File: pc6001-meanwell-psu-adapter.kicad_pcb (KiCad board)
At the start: 2 copper layers, 223.7 x 84 mm, 4 parts

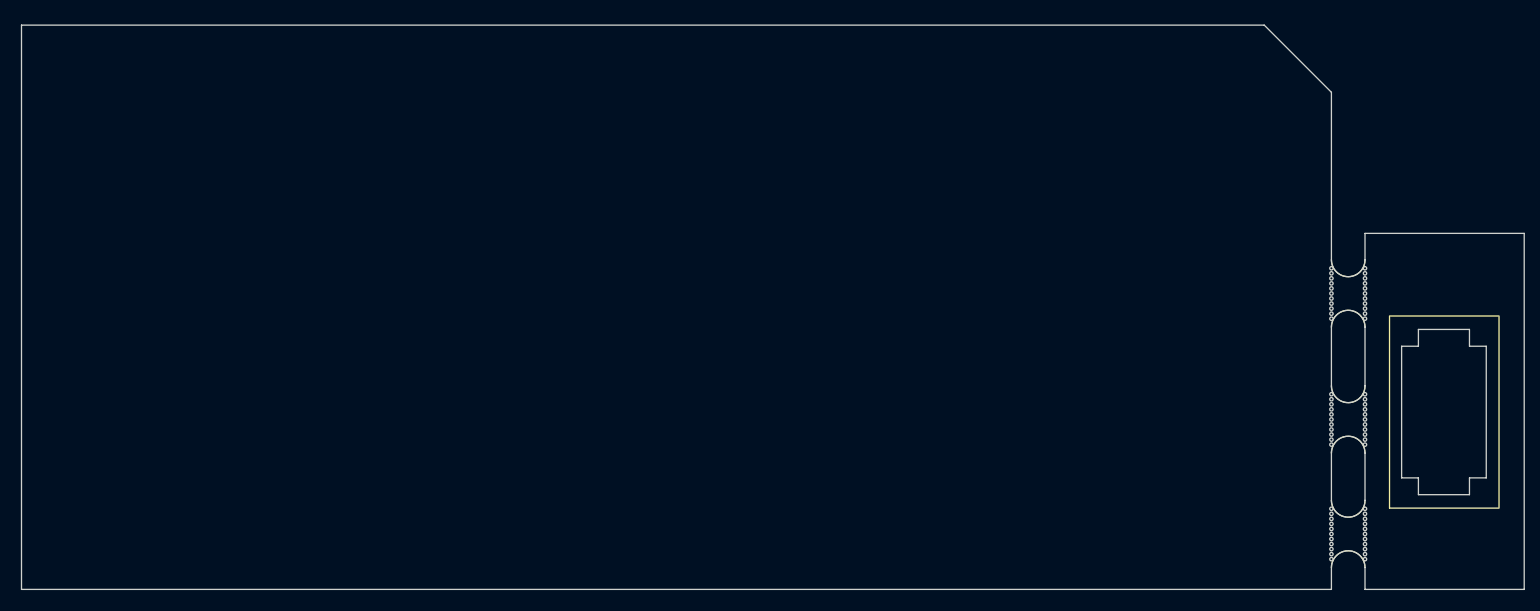
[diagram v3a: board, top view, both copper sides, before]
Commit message: Mounting holes
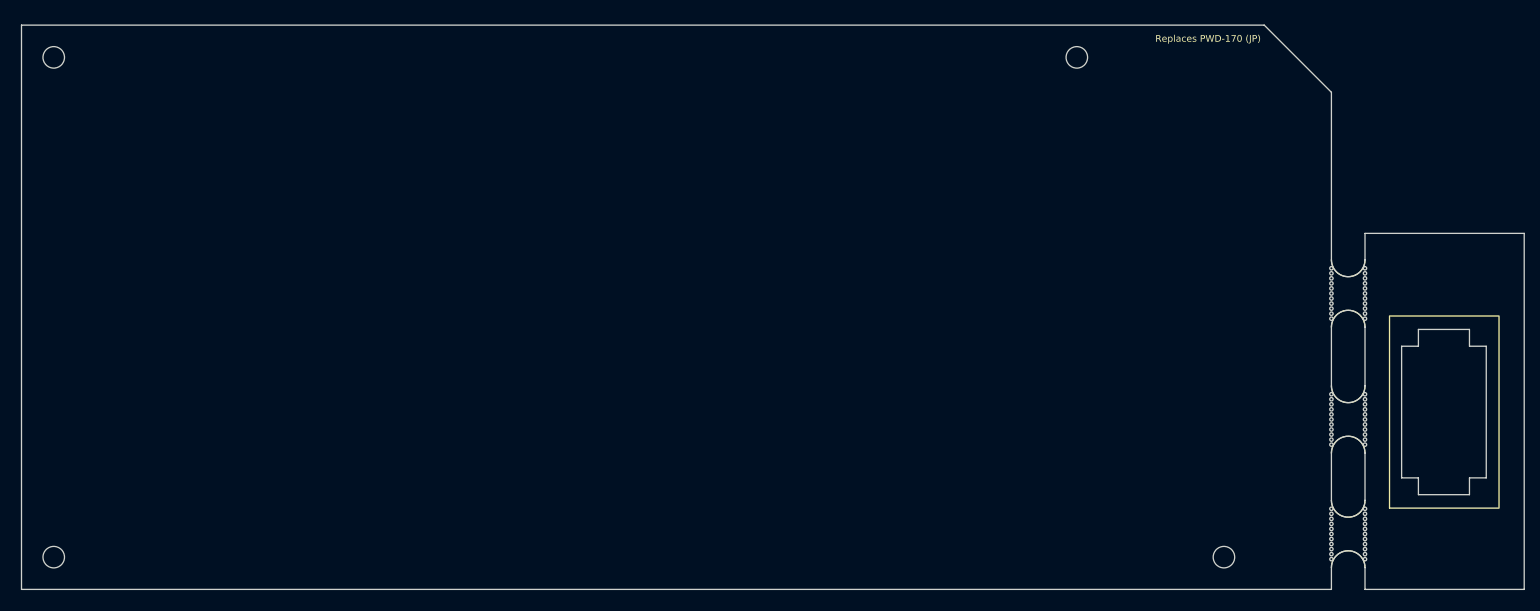
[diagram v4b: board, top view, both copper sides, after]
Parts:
- added REF**: MountingHole_3.2mm_M3_DIN965, MountingHole:MountingHole_3.2mm_M3_DIN965, F.Cu at (56.8, 54.8)
- added REF**: MountingHole_3.2mm_M3_DIN965, MountingHole:MountingHole_3.2mm_M3_DIN965, F.Cu at (56.8, 129.2)
- added REF**: MountingHole_3.2mm_M3_DIN965, MountingHole:MountingHole_3.2mm_M3_DIN965, F.Cu at (231.0, 129.2)
- added REF**: MountingHole_3.2mm_M3_DIN965, MountingHole:MountingHole_3.2mm_M3_DIN965, F.Cu at (209.1, 54.8)
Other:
- board text added: "Replaces PWD-170 (JP)"
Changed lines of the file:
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@@
   )
   (net 0 "")
-  (footprint "PowerEntry:Qualitek_770W-X2-13_IEC_C8" (layer "F.Cu")
+  (footprint "PowerEntry:Qualitek_770W-X2-13_IEC_C8" locked (layer "F.Cu")
     (at 273.55 109.1 90)
     (fp_text reference "REF**" (at 0 -0.5 90 unlocked) (layer "F.SilkS") hide
@@
     (fp_line (start 13.8 -6) (end 13.8 -13.6)
       (stroke (width 0.05) (type default)) (layer "Edge.Cuts"))
+  )
+  (footprint "MountingHole:MountingHole_3.2mm_M3_DIN965" (layer "F.Cu")
+    (at 56.8 54.8)
+    (descr "Mounting Hole 3.2mm, no annular, M3, DIN965")
+    (tags "mounting hole 3.2mm no annular m3 din965")
+    (attr exclude_from_pos_files exclude_from_bom)
+    (fp_text reference "REF**" (at 0 -3.8) (layer "F.SilkS") hide
+        (effects (font (size 1 1) (thickness 0.15)))
+    )
+    (fp_text value "MountingHole_3.2mm_M3_DIN965" (at 0 3.8) (layer "F.Fab")
+        (effects (font (size 1 1) (thickness 0.15)))
+    )
+    (fp_text user "${REFERENCE}" (at 0 0) (layer "F.Fab")
+        (effects (font (size 1 1) (thickness 0.15)))
+    )
+    (fp_circle (center 0 0) (end 2.8 0)
+      (stroke (width 0.15) (type solid)) (fill none) (layer "Cmts.User"))
+    (fp_circle (center 0 0) (end 3.05 0)
+      (stroke (width 0.05) (type solid)) (fill none) (layer "F.CrtYd"))
+    (pad "" np_thru_hole circle (at 0 0) (size 3.2 3.2) (drill 3.2) (layers "*.Cu" "*.Mask"))
+  )
+  (footprint "MountingHole:MountingHole_3.2mm_M3_DIN965" (layer "F.Cu")
+    (at 56.8 129.2)
+    (descr "Mounting Hole 3.2mm, no annular, M3, DIN965")
+    (tags "mounting hole 3.2mm no annular m3 din965")
+    (attr exclude_from_pos_files exclude_from_bom)
+    (fp_text reference "REF**" (at 0 -3.8) (layer "F.SilkS") hide
+        (effects (font (size 1 1) (thickness 0.15)))
+    )
+    (fp_text value "MountingHole_3.2mm_M3_DIN965" (at 0 3.8) (layer "F.Fab")
+        (effects (font (size 1 1) (thickness 0.15)))
+    )
+    (fp_text user "${REFERENCE}" (at 0 0) (layer "F.Fab")
+        (effects (font (size 1 1) (thickness 0.15)))
+    )
+    (fp_circle (center 0 0) (end 2.8 0)
+      (stroke (width 0.15) (type solid)) (fill none) (layer "Cmts.User"))
+    (fp_circle (center 0 0) (end 3.05 0)
+      (stroke (width 0.05) (type solid)) (fill none) (layer "F.CrtYd"))
+    (pad "" np_thru_hole circle (at 0 0) (size 3.2 3.2) (drill 3.2) (layers "*.Cu" "*.Mask"))
   )
   (footprint "Panelization.pretty-master:mouse-bite-5mm-slot" (layer "F.Cu")
@@
     (pad "" np_thru_hole circle (at 3.75 2.5 90) (size 0.5 0.5) (drill 0.5) (layers "*.Cu" "*.Mask"))
   )
+  (footprint "MountingHole:MountingHole_3.2mm_M3_DIN965" (layer "F.Cu")
+    (at 231 129.2)
+    (descr "Mounting Hole 3.2mm, no annular, M3, DIN965")
+    (tags "mounting hole 3.2mm no annular m3 din965")
+    (attr exclude_from_pos_files exclude_from_bom)
+    (fp_text reference "REF**" (at 0 -3.8) (layer "F.SilkS") hide
+        (effects (font (size 1 1) (thickness 0.15)))
+    )
+    (fp_text value "MountingHole_3.2mm_M3_DIN965" (at 0 3.8) (layer "F.Fab")
+        (effects (font (size 1 1) (thickness 0.15)))
+    )
+    (fp_text user "${REFERENCE}" (at 0 0) (layer "F.Fab")
+        (effects (font (size 1 1) (thickness 0.15)))
+    )
+    (fp_circle (center 0 0) (end 2.8 0)
+      (stroke (width 0.15) (type solid)) (fill none) (layer "Cmts.User"))
+    (fp_circle (center 0 0) (end 3.05 0)
+      (stroke (width 0.05) (type solid)) (fill none) (layer "F.CrtYd"))
+    (pad "" np_thru_hole circle (at 0 0) (size 3.2 3.2) (drill 3.2) (layers "*.Cu" "*.Mask"))
+  )
+  (footprint "MountingHole:MountingHole_3.2mm_M3_DIN965" (layer "F.Cu")
+    (at 209.1 54.8)
+    (descr "Mounting Hole 3.2mm, no annular, M3, DIN965")
+    (tags "mounting hole 3.2mm no annular m3 din965")
+    (attr exclude_from_pos_files exclude_from_bom)
+    (fp_text reference "REF**" (at 0 -3.8) (layer "F.SilkS") hide
+        (effects (font (size 1 1) (thickness 0.15)))
+    )
+    (fp_text value "MountingHole_3.2mm_M3_DIN965" (at 0 3.8) (layer "F.Fab")
+        (effects (font (size 1 1) (thickness 0.15)))
+    )
+    (fp_text user "${REFERENCE}" (at 0 0) (layer "F.Fab")
+        (effects (font (size 1 1) (thickness 0.15)))
+    )
+    (fp_circle (center 0 0) (end 2.8 0)
+      (stroke (width 0.15) (type solid)) (fill none) (layer "Cmts.User"))
+    (fp_circle (center 0 0) (end 3.05 0)
+      (stroke (width 0.05) (type solid)) (fill none) (layer "F.CrtYd"))
+    (pad "" np_thru_hole circle (at 0 0) (size 3.2 3.2) (drill 3.2) (layers "*.Cu" "*.Mask"))
+  )
   (gr_line (start 252 81) (end 275.7 81)
     (stroke (width 0.1) (type default)) (layer "Edge.Cuts"))
@@
   (gr_line (start 237 50) (end 247 60)
     (stroke (width 0.1) (type default)) (layer "Edge.Cuts"))
+  (gr_text "Replaces PWD-170 (JP)" (at 236.5 52.6) (layer "F.SilkS")
+    (effects (font (size 1 1) (thickness 0.15)) (justify right bottom))
+  )
   (gr_text "TODO: make smaller if possible" (at 137 130) (layer "Cmts.User")
     (effects (font (size 1 1) (thickness 0.15)) (justify left bottom))
@@
   (gr_text "TODO: measure mounting holes" (at 137 132) (layer "Cmts.User")
     (effects (font (size 1 1) (thickness 0.15)) (justify left bottom))
+  )
+  (dimension (type aligned) (layer "Cmts.User")
+    (pts (xy 242 55) (xy 209 55))
+    (height 61.5)
+    (gr_text "33.0000 mm" (at 225.5 -7.65) (layer "Cmts.User")
+      (effects (font (size 1 1) (thickness 0.15)))
+    )
+    (format (prefix "") (suffix "") (units 3) (units_format 1) (precision 4))
+    (style (thickness 0.15) (arrow_length 1.27) (text_position_mode 0) (extension_height 0.58642) (extension_offset 0.5) keep_text_aligned)
   )
   (dimension (type aligned) (layer "Cmts.User")
@@
   )
   (dimension (type aligned) (layer "Cmts.User")
+    (pts (xy 52 134) (xy 52 129.2))
+    (height 270)
+    (gr_text "4.8000 mm" (at 320.85 131.6 90) (layer "Cmts.User")
+      (effects (font (size 1 1) (thickness 0.15)))
+    )
+    (format (prefix "") (suffix "") (units 3) (units_format 1) (precision 4))
+    (style (thickness 0.15) (arrow_length 1.27) (text_position_mode 0) (extension_height 0.58642) (extension_offset 0.5) keep_text_aligned)
+  )
+  (dimension (type aligned) (layer "Cmts.User")
+    (pts (xy 237 50) (xy 237 54.8))
+    (height 232.1)
+    (gr_text "4.8000 mm" (at 3.75 52.4 90) (layer "Cmts.User")
+      (effects (font (size 1 1) (thickness 0.15)))
+    )
+    (format (prefix "") (suffix "") (units 3) (units_format 1) (precision 4))
+    (style (thickness 0.15) (arrow_length 1.27) (text_position_mode 0) (extension_height 0.58642) (extension_offset 0.5) keep_text_aligned)
+  )
+  (dimension (type aligned) (layer "Cmts.User")
     (pts (xy 52 134) (xy 247 134))
     (height 25)
@@
       (effects (font (size 1 1) (thickness 0.15)))
     )
+    (format (prefix "") (suffix "") (units 3) (units_format 1) (precision 4))
+    (style (thickness 0.15) (arrow_length 1.27) (text_position_mode 0) (extension_height 0.58642) (extension_offset 0.5) keep_text_aligned)
+  )
+  (dimension (type aligned) (layer "Cmts.User")
+    (pts (xy 52 50) (xy 56.8 50))
+    (height 157.2)
+    (gr_text "4.8000 mm" (at 54.4 206.05) (layer "Cmts.User")
+      (effects (font (size 1 1) (thickness 0.15)))
+    )
+    (format (prefix "") (suffix "") (units 3) (units_format 1) (precision 4))
+    (style (thickness 0.15) (arrow_length 1.27) (text_position_mode 0) (extension_height 0.58642) (extension_offset 0.5) keep_text_aligned)
+  )
+  (dimension (type aligned) (layer "Cmts.User")
+    (pts (xy 247 134) (xy 231 134))
+    (height 128.9)
+    (gr_text "16.0000 mm" (at 239 3.95) (layer "Cmts.User")
+      (effects (font (size 1 1) (thickness 0.15)))
+    )

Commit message: Made a footprint
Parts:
- removed the REF** at (273.6, 109.1)
- removed mouse-bite-5mm-slot (x3): VAL**, Panelization.pretty-master:mouse-bite-5mm-slot
- added J1: Meanwell RPT-60B PSU module, Meanwell:RPT-60, F.Cu at (95.2, 66.8)
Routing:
- added copper zone on B.Cu, net GND
- added copper zone on F.Cu, net GND
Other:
- board size 223.7 x 84 mm -> 195 x 84 mm
- board text added: "Attach safety ground with ring terminal to chassis"
- board text added: "PC-6001 Meanwell Adapter"
- board text added: "Replaces: PWD-170 (JP) PWD-270 (US)"
- board text added: "TODO: What about the cartridge slot safety defeat?"
- board text added: "leadedsolder.com 2024, version 1"
- board text removed: "Replaces PWD-170 (JP)"

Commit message: V1 to fab
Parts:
- REF** (x4): value MountingHole_3.2mm_M3_DIN965 -> MountingHole_3.5mm_Pad; footprint MountingHole:MountingHole_3.2mm_M3_DIN965 -> MountingHole:MountingHole_3.5mm_Pad
- moved J1 15.9 mm to (111.1, 66.8)
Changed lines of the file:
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@@
 			(outputformat 1)
 			(mirror no)
-			(drillshape 1)
+			(drillshape 0)
 			(scaleselection 1)
-			(outputdirectory "")
+			(outputdirectory "pc6001-rpt60b-v1")
 		)
 	)
@@
 	(footprint "Meanwell:RPT-60"
 		(layer "F.Cu")
-		(at 95.25 66.775)
+		(at 111.125 66.775)
 		(property "Reference" "J1"
 			(at 50.8 23.57 0)
@@
 		)
 	)
-	(footprint "MountingHole:MountingHole_3.2mm_M3_DIN965"
+	(footprint "MountingHole:MountingHole_3.5mm_Pad"
 		(layer "F.Cu")
 		(at 56.8 54.8)
-		(descr "Mounting Hole 3.2mm, no annular, M3, DIN965")
-		(tags "mounting hole 3.2mm no annular m3 din965")
+		(descr "Mounting Hole 3.5mm")
+		(tags "mounting hole 3.5mm")
 		(property "Reference" "REF**"
-			(at 0 -3.8 0)
+			(at 0 -4.5 0)
 			(layer "F.SilkS")
 			(hide yes)
@@
 			)
 		)
-		(property "Value" "MountingHole_3.2mm_M3_DIN965"
-			(at 0 3.8 0)
-			(layer "F.Fab")
-			(effects
-				(font
-					(size 1 1)
-					(thickness 0.15)
-				)
-			)
-		)
-		(property "Footprint" ""
-			(at 0 0 0)
+		(property "Value" "MountingHole_3.5mm_Pad"
+			(at 0 4.5 0)
+			(layer "F.Fab")
+			(effects
+				(font
+					(size 1 1)
+					(thickness 0.15)
+				)
+			)
+		)
+		(property "Footprint" "MountingHole:MountingHole_3.5mm_Pad"
+			(at 0 0 0)
+			(unlocked yes)
 			(layer "F.Fab")
 			(hide yes)
@@
 		(property "Datasheet" ""
 			(at 0 0 0)
+			(unlocked yes)
 			(layer "F.Fab")
 			(hide yes)
@@
 		(property "Description" ""
 			(at 0 0 0)
+			(unlocked yes)
 			(layer "F.Fab")
 			(hide yes)
@@
 		(fp_circle
 			(center 0 0)
-			(end 2.8 0)
+			(end 3.5 0)
 			(stroke
 				(width 0.15)
@@
 		(fp_circle
 			(center 0 0)
-			(end 3.05 0)
+			(end 3.75 0)
 			(stroke
 				(width 0.05)
@@
 			)
 		)
-		(pad "" np_thru_hole circle
+		(pad "1" thru_hole circle
 			(at 0 0)
-			(size 3.2 3.2)
-			(drill 3.2)
-			(layers "*.Cu" "*.Mask")
-		)
-	)
-	(footprint "MountingHole:MountingHole_3.2mm_M3_DIN965"
+			(size 7 7)
+			(drill 3.5)
+			(layers "*.Cu" "*.Mask")
+			(remove_unused_layers no)
+			(net 1 "GND")
+		)
+	)
+	(footprint "MountingHole:MountingHole_3.5mm_Pad"
 		(layer "F.Cu")
 		(at 56.8 129.2)
-		(descr "Mounting Hole 3.2mm, no annular, M3, DIN965")
-		(tags "mounting hole 3.2mm no annular m3 din965")
+		(descr "Mounting Hole 3.5mm")
+		(tags "mounting hole 3.5mm")
 		(property "Reference" "REF**"
-			(at 0 -3.8 0)
+			(at 0 -4.5 0)
 			(layer "F.SilkS")
 			(hide yes)
@@
 			)
 		)
-		(property "Value" "MountingHole_3.2mm_M3_DIN965"
-			(at 0 3.8 0)
-			(layer "F.Fab")
-			(effects
-				(font
-					(size 1 1)
-					(thickness 0.15)
-				)
-			)
-		)
-		(property "Footprint" ""
-			(at 0 0 0)
+		(property "Value" "MountingHole_3.5mm_Pad"
+			(at 0 4.5 0)
+			(layer "F.Fab")
+			(effects
+				(font
+					(size 1 1)
+					(thickness 0.15)
+				)
+			)
+		)
+		(property "Footprint" "MountingHole:MountingHole_3.5mm_Pad"
+			(at 0 0 0)
+			(unlocked yes)
 			(layer "F.Fab")
 			(hide yes)
@@
 		(property "Datasheet" ""
 			(at 0 0 0)
+			(unlocked yes)
 			(layer "F.Fab")
 			(hide yes)
@@
 		(property "Description" ""
 			(at 0 0 0)
+			(unlocked yes)
 			(layer "F.Fab")
 			(hide yes)
@@
 		(fp_circle
 			(center 0 0)
-			(end 2.8 0)
+			(end 3.5 0)
 			(stroke
 				(width 0.15)
@@
 		(fp_circle
 			(center 0 0)
-			(end 3.05 0)
+			(end 3.75 0)
 			(stroke
 				(width 0.05)
@@
 			)
 		)
-		(pad "" np_thru_hole circle
+		(pad "1" thru_hole circle
 			(at 0 0)
-			(size 3.2 3.2)
-			(drill 3.2)
-			(layers "*.Cu" "*.Mask")
-		)
-	)
-	(footprint "MountingHole:MountingHole_3.2mm_M3_DIN965"
+			(size 7 7)
+			(drill 3.5)
+			(layers "*.Cu" "*.Mask")
+			(remove_unused_layers no)
+			(net 1 "GND")
+		)
+	)
+	(footprint "MountingHole:MountingHole_3.5mm_Pad"
 		(layer "F.Cu")
 		(at 231 129.2)
-		(descr "Mounting Hole 3.2mm, no annular, M3, DIN965")
-		(tags "mounting hole 3.2mm no annular m3 din965")
+		(descr "Mounting Hole 3.5mm")
+		(tags "mounting hole 3.5mm")
 		(property "Reference" "REF**"
-			(at 0 -3.8 0)
+			(at 0 -4.5 0)
 			(layer "F.SilkS")
 			(hide yes)
@@
 			)
 		)
-		(property "Value" "MountingHole_3.2mm_M3_DIN965"
-			(at 0 3.8 0)
-			(layer "F.Fab")
-			(effects
-				(font
-					(size 1 1)
-					(thickness 0.15)
-				)
-			)
-		)
-		(property "Footprint" ""
-			(at 0 0 0)
+		(property "Value" "MountingHole_3.5mm_Pad"
+			(at 0 4.5 0)
+			(layer "F.Fab")
+			(effects
+				(font
+					(size 1 1)
+					(thickness 0.15)
+				)
+			)
+		)
+		(property "Footprint" "MountingHole:MountingHole_3.5mm_Pad"
+			(at 0 0 0)
+			(unlocked yes)
 			(layer "F.Fab")
 			(hide yes)
@@
 		(property "Datasheet" ""
 			(at 0 0 0)
+			(unlocked yes)
 			(layer "F.Fab")
 			(hide yes)
@@
 		(property "Description" ""
 			(at 0 0 0)
+			(unlocked yes)
 			(layer "F.Fab")
 			(hide yes)
@@
 		(fp_circle
 			(center 0 0)
-			(end 2.8 0)
+			(end 3.5 0)
 			(stroke
 				(width 0.15)
@@
 		(fp_circle
 			(center 0 0)
-			(end 3.05 0)
+			(end 3.75 0)
 			(stroke
 				(width 0.05)
@@
 			)
 		)
-		(pad "" np_thru_hole circle
+		(pad "1" thru_hole circle
 			(at 0 0)
-			(size 3.2 3.2)
-			(drill 3.2)
-			(layers "*.Cu" "*.Mask")
-		)
-	)
-	(footprint "MountingHole:MountingHole_3.2mm_M3_DIN965"
+			(size 7 7)
+			(drill 3.5)
+			(layers "*.Cu" "*.Mask")
+			(remove_unused_layers no)
+			(net 1 "GND")
+		)
+	)
+	(footprint "MountingHole:MountingHole_3.5mm_Pad"
 		(layer "F.Cu")
 		(at 209.1 54.8)
-		(descr "Mounting Hole 3.2mm, no annular, M3, DIN965")
-		(tags "mounting hole 3.2mm no annular m3 din965")
+		(descr "Mounting Hole 3.5mm")
+		(tags "mounting hole 3.5mm")
 		(property "Reference" "REF**"
-			(at 0 -3.8 0)
+			(at 0 -4.5 0)
 			(layer "F.SilkS")
 			(hide yes)
@@
 			)
 		)
-		(property "Value" "MountingHole_3.2mm_M3_DIN965"
-			(at 0 3.8 0)
-			(layer "F.Fab")
-			(effects
-				(font
-					(size 1 1)
-					(thickness 0.15)
-				)
-			)
-		)
-		(property "Footprint" ""
-			(at 0 0 0)
+		(property "Value" "MountingHole_3.5mm_Pad"
+			(at 0 4.5 0)
+			(layer "F.Fab")
+			(effects
+				(font
+					(size 1 1)
+					(thickness 0.15)
+				)
+			)
+		)
+		(property "Footprint" "MountingHole:MountingHole_3.5mm_Pad"
+			(at 0 0 0)
+			(unlocked yes)
 			(layer "F.Fab")
 			(hide yes)
@@
 		(property "Datasheet" ""
 			(at 0 0 0)
+			(unlocked yes)
 			(layer "F.Fab")
 			(hide yes)
@@
 		(property "Description" ""
 			(at 0 0 0)
+			(unlocked yes)
 			(layer "F.Fab")
 			(hide yes)
@@
 		(fp_circle
 			(center 0 0)
-			(end 2.8 0)
+			(end 3.5 0)
 			(stroke
 				(width 0.15)
@@
 		(fp_circle
 			(center 0 0)
-			(end 3.05 0)
+			(end 3.75 0)
 			(stroke
 				(width 0.05)
@@
 			)
 		)
-		(pad "" np_thru_hole circle
+		(pad "1" thru_hole circle
 			(at 0 0)
-			(size 3.2 3.2)
-			(drill 3.2)
-			(layers "*.Cu" "*.Mask")
+			(size 7 7)
+			(drill 3.5)
+			(layers "*.Cu" "*.Mask")
+			(remove_unused_layers no)
+			(net 1 "GND")
 		)
 	)
@@
 	)
 	(gr_text "Attach safety ground with ring terminal to chassis"
-		(at 102.87 114.935 0)
+		(at 118.745 114.935 0)
 		(layer "F.SilkS")
 		(effects
@@
 	)
 	(gr_text "leadedsolder.com 2024, version 1"
-		(at 63.5 132.715 0)
+		(at 61.595 132.08 0)
 		(layer "F.SilkS")
 		(effects
 			(font
 				(size 1 1)
-				(thickness 0.15)
+				(thickness 0.2)
+				(bold yes)
 			)
 			(justify left bottom)
